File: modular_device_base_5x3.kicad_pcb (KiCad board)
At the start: 2 copper layers, 83.8 x 40.6 mm, 23 parts, among them P1 PWR_JACK_2.5x5.5_SMD_RA, P2 HEADER_01X03_SMD_RA, P3 HEADER_01X03_SMD_RA, P4 HEADER_01X03_SMD_RA, P5 BNC_DOUBLE_RA, P6 HEADER_01X02_SMD_RA, P7 HEADER_01X02_SMD_RA, SW1 KT_SWITCH

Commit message: footprints: -> modular_device_base_5x3:.
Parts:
- MDB1: footprint footprints:MODULAR_DEVICE_BASE_5X3_FEMALE -> modular_device_base_5x3:MODULAR_DEVICE_BASE_5X3_FEMALE
- TEENSY1: footprint footprints:TEENSY_3.2 -> modular_device_base_5x3:TEENSY_3.2
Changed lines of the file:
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@@
     (pad 1 thru_hole circle (at 0 0) (size 3.556 3.556) (drill 3.302) (layers *.Cu *.Mask F.SilkS))
   )
-  (module footprints:MODULAR_DEVICE_BASE_5X3_FEMALE (layer F.Cu)
+  (module modular_device_base_5x3:MODULAR_DEVICE_BASE_5X3_FEMALE (layer F.Cu)
     (at 95.25 99.695)
     (fp_text reference MDB1 (at 0 0) (layer F.SilkS) hide
@@
     (pad "" thru_hole circle (at 22.86 -17.78) (size 3.556 3.556) (drill 3.302) (layers *.Cu *.Mask F.SilkS))
   )
-  (module footprints:TEENSY_3.2 (layer B.Cu)
+  (module modular_device_base_5x3:TEENSY_3.2 (layer B.Cu)
     (at 95.25 99.695 270)
     (fp_text reference TEENSY1 (at 0 -19.05 270) (layer B.SilkS)

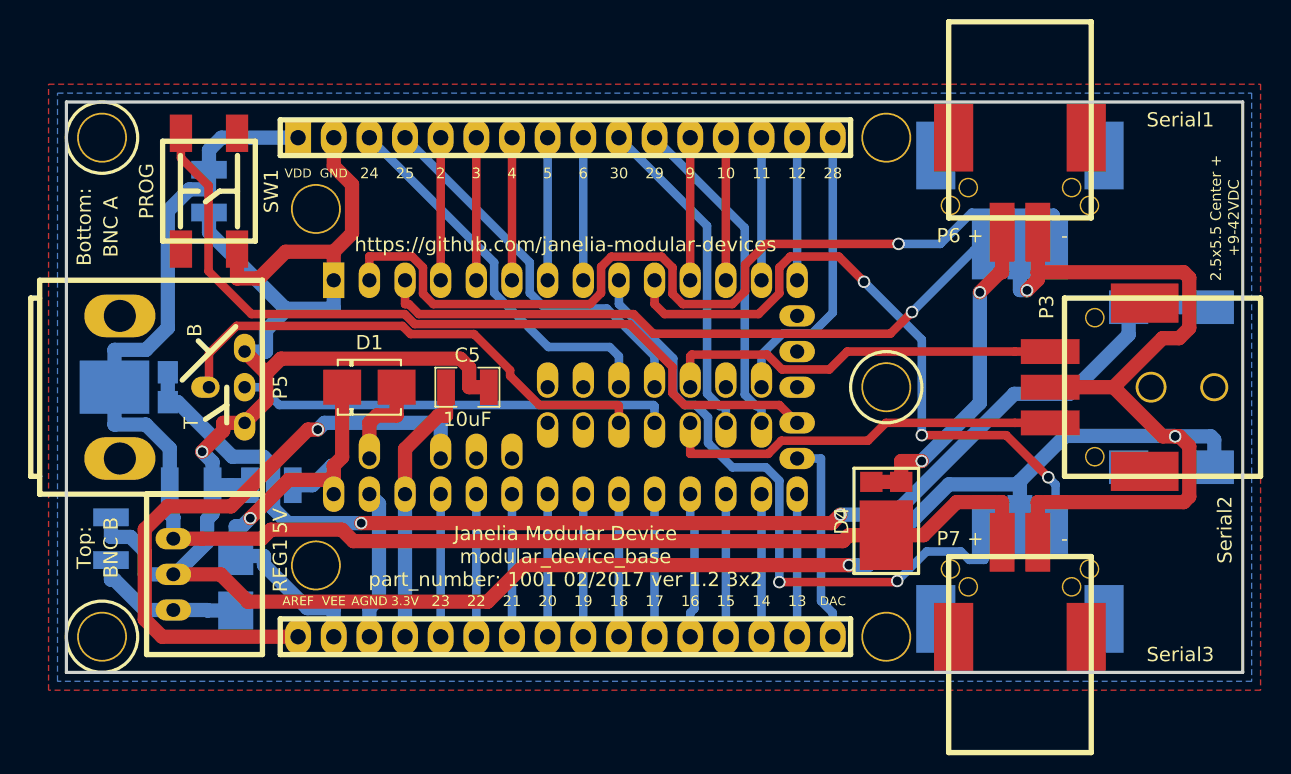
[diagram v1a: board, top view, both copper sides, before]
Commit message: Added TEENSY_3.5 footprint.
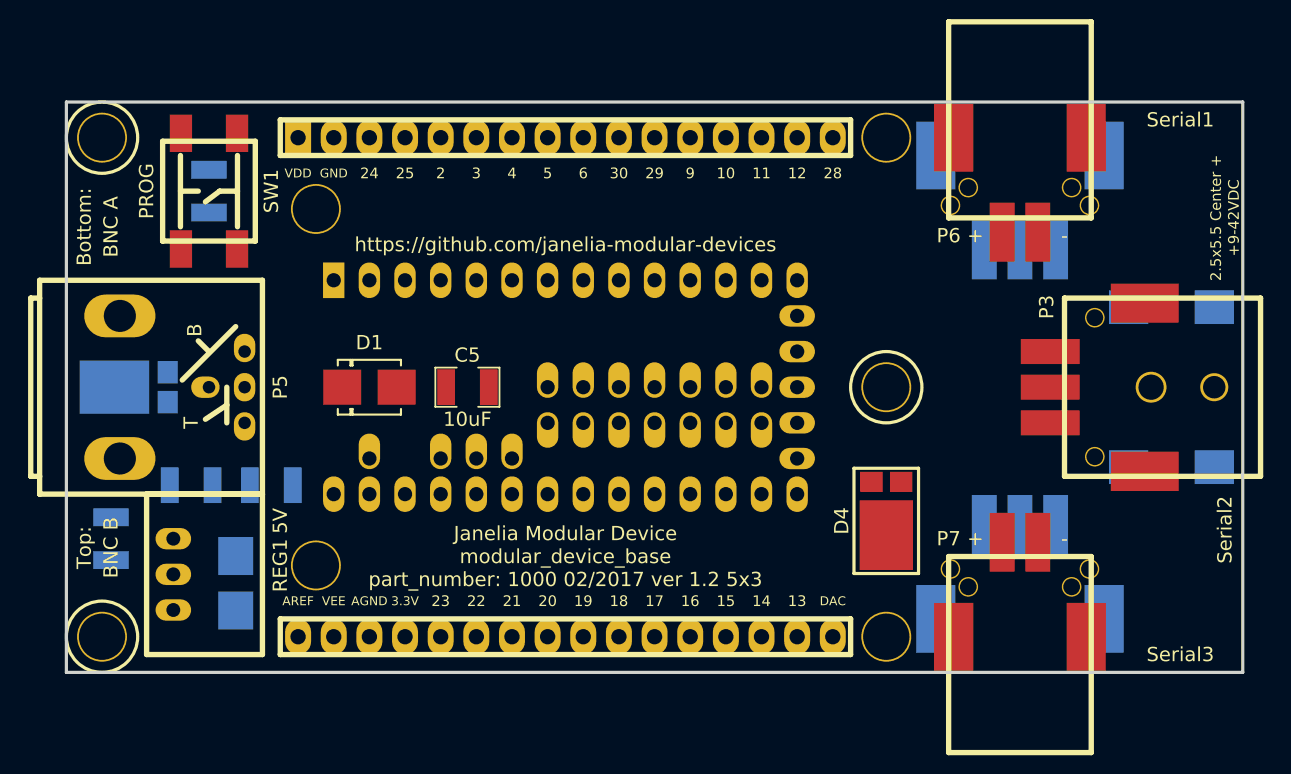
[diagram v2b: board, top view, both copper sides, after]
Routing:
- net GND: track 233.6 -> 0.00 mm, vias 4 -> 0
- net VDD: track 106.1 -> 0.00 mm
- net VAA: track 89.5 -> 0.00 mm, vias 2 -> 0
- net /RX1: track 64.5 -> 0.00 mm, vias 1 -> 0
- net /PROG: track 58.2 -> 0.00 mm
- net /TX3: track 46.9 -> 0.00 mm, vias 3 -> 0
- net /RX3: track 46.4 -> 0.00 mm, vias 2 -> 0
- net /TX1: track 46.3 -> 0.00 mm, vias 1 -> 0
- net /AREF: track 44.6 -> 0.00 mm, vias 1 -> 0
- net /BNC_A: track 36.2 -> 0.00 mm
- net VEE: track 34.8 -> 0.00 mm, vias 1 -> 0
- net /BNC_B: track 31.0 -> 0.00 mm
- net /RX2: track 28.9 -> 0.00 mm
- net /TX2: track 28.8 -> 0.00 mm
- net /D25: track 27.7 -> 0.00 mm
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- removed copper zone on B.Cu, net GND
- removed copper zone on F.Cu, net GND
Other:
- board text added: "Janelia Modular Device modular_device_base part_number: 1000 02/2017 ver 1.2 5x3"
- board text removed: "Janelia Modular Device modular_device_base part_number: 1001 02/2017 ver 1.2 3x2"

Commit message: Progress towards new modifications.
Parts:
- added D5: diode_schottky_45V_10A, modular_device_base_5x3:CFP15, F.Cu at (171.4, 99.7)
- added E1: TEENSY_ETHERNET, footprints:TEENSY_ETHERNET, B.Cu at (153.0, 84.5)
- added MH4: MNT_HOLE, modular_device_base_5x3:MOUNTING_HOLE_4-40, F.Cu at (141.0, 121.9)
- added P10: HEADER_01X02_SMD_RA, modular_device_base_5x3:Header_2_Pin_SMD_RA, F.Cu at (62.2, 83.8)
- added P8: HEADER_01X02_SMD_RA, modular_device_base_5x3:Header_2_Pin_SMD_RA, F.Cu at (191.8, 84.5)
- added P9: HEADER_01X03_SMD_RA, modular_device_base_5x3:Header_3_Pin_SMD_RA, B.Cu at (63.5, 83.8)
- D3: moved to F.Cu
- MDB1: value modular_device_base_5x3_FEMALE -> MODULAR_DEVICE_BASE_5x3_FEMALE; footprint modular_device_base_5x3:MODULAR_DEVICE_BASE_5X3_FEMALE -> footprints:MODULAR_DEVICE_BASE_5X3_FEMALE
- P1: value PWR_JACK_2.5x5.5_SMD_RA -> PWR_JACK_2.5x5.5; footprint modular_device_base_5x3:DCJACK_2PIN_HIGHCURRENT_SMD_RA -> footprints:DCJACK_2PIN_HIGHCURRENT
- P2: value HEADER_01X03_SMD_RA -> BNC_DOUBLE_RA; footprint modular_device_base_5x3:Header_3_Pin_SMD_RA -> modular_device_base_5x3:BNC_DOUBLE; moved to F.Cu
- P3: moved to B.Cu
- P4: value HEADER_01X03_SMD_RA -> HEADER_01X02_SMD_RA; footprint modular_device_base_5x3:Header_3_Pin_SMD_RA -> modular_device_base_5x3:Header_2_Pin_SMD_RA; moved to F.Cu
- P5: value BNC_DOUBLE_RA -> HEADER_01X03_SMD_RA; footprint modular_device_base_5x3:BNC_DOUBLE -> modular_device_base_5x3:Header_3_Pin_SMD_RA; moved to B.Cu
- P7: value HEADER_01X02_SMD_RA -> HEADER_01X03_SMD_RA; footprint modular_device_base_5x3:Header_2_Pin_SMD_RA -> modular_device_base_5x3:Header_3_Pin_SMD_RA; moved to B.Cu
- TEENSY1: value TEENSY_3_2 -> TEENSY_3.5; footprint modular_device_base_5x3:TEENSY_3.2 -> footprints:TEENSY_3.5
- moved P5 119.2 mm to (179.1, 128.9), turned to 0 degrees
- moved D3 112.4 mm to (176.5, 99.7), turned to 0 degrees
- moved P7 71.0 mm to (190.5, 84.5), turned to 90 degrees
- moved P6 70.5 mm to (179.1, 130.2), turned to 180 degrees
- moved P4 69.2 mm to (178.4, 69.2)
- moved P2 66.2 mm to (63.5, 99.7), turned to 90 degrees
- moved P1 55.9 mm to (194.3, 99.7), turned to 90 degrees
- moved P3 51.1 mm to (178.4, 70.5), turned to 180 degrees
- moved D4 49.2 mm to (166.4, 99.7)
- moved MH3 31.9 mm to (141.0, 77.5)
- moved C3 13.3 mm to (69.8, 72.4)
- moved SW1 13.3 mm to (69.8, 72.4)
- moved MH2 12.7 mm to (62.2, 130.2)
- moved MH1 12.7 mm to (62.2, 69.2)
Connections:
- P2 pad 1: /RX1 -> /BNC_A
- P2 pad 3: /TX1 -> /BNC_B
- P3 pad 1: /RX2 -> /RX1
- P3 pad 3: /TX2 -> /TX1
- P4 pad 1: /RX3 -> VCC
- P5 pad 1: /BNC_A -> /RX3
- P5 pad 3: /BNC_B -> /TX3
- P6 pad 1: VCC -> GND
- P6 pad 2: GND -> VDD
- P7 pad 1: GND -> /RX2
- P7 pad 2: VDD -> GND
- TEENSY1 pad 10: /D10 -> /TX2
- TEENSY1 pad 24: /D24 -> /E_CLK
- TEENSY1 pad 25: /D25 -> /E_RXER
- TEENSY1 pad 26: /RX2 -> /E_RXDV
- TEENSY1 pad 27: (no net) -> /E_TXEN
- TEENSY1 pad 28: /D28 -> /E_TXD0
- TEENSY1 pad 3: /D3 -> /E_RXD1
- TEENSY1 pad 31: /TX2 -> /RX4
- TEENSY1 pad 32: /BNC_B -> /TX4
- TEENSY1 pad 33: /BNC_A -> /D33
- TEENSY1 pad 4: /D4 -> /E_RXD0
- TEENSY1 pad 9: /D9 -> /RX2
- TEENSY1 pad A10: (no net) -> /A10
- TEENSY1 pad A11: (no net) -> /A11
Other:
- board size 83.8 x 40.6 mm -> 134.6 x 66 mm

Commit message: Finished design ver 1.0.
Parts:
- moved MH3 51.5 mm to (191.8, 69.2)
- moved MH4 51.5 mm to (191.8, 130.2)
- moved D4 10.4 mm to (174.6, 93.3), turned to 270 degrees
- moved D3 6.63 mm to (174.6, 106.0), turned to 270 degrees
- moved E1 6.35 mm to (159.4, 84.5)
- moved D5 3.18 mm to (174.6, 99.7), turned to 270 degrees
- moved P7 0.64 mm to (190.5, 83.8)
- moved P8 0.64 mm to (191.8, 83.8)
- moved P5 0.63 mm to (178.4, 128.9)
- moved P6 0.63 mm to (178.4, 130.2)
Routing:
- net GND: track 0.00 -> 337.7 mm, vias 0 -> 4
- net VDD: track 0.00 -> 206.6 mm, vias 0 -> 2
- net /RX1: track 0.00 -> 110.5 mm, vias 0 -> 1
- net /TX2: track 0.00 -> 106.8 mm, vias 0 -> 1
- net /TX1: track 0.00 -> 103.2 mm, vias 0 -> 1
- net /TX3: track 0.00 -> 95.7 mm, vias 0 -> 1
- net /RX3: track 0.00 -> 93.5 mm, vias 0 -> 1
- net /RX4: track 0.00 -> 91.0 mm, vias 0 -> 2
- net /PROG: track 0.00 -> 86.7 mm
- net /E_RXD1: track 0.00 -> 84.9 mm
- net /RX2: track 0.00 -> 83.0 mm, vias 0 -> 1
- net /TX4: track 0.00 -> 82.7 mm, vias 0 -> 2
- net /E_RXD0: track 0.00 -> 81.3 mm
- net /E_RXDV: track 0.00 -> 61.1 mm
- net /E_RXER: track 0.00 -> 60.4 mm
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- added copper zone on B.Cu, net GND
- added copper zone on F.Cu, net VDD
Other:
- net class Power: trace_width 1.016 -> 1.2192
- board text added: "2.5x5.5 Center + +9-42VDC"
- board text added: "BNC A"
- board text added: "BNC B"
- board text added: "Janelia Modular Device modular_device_base part_number: 1000 02/2017 ver 1.0 5x3"
- board text added: "Serial4"
- board text removed: "+9-42VDC"
- board text removed: "2.5x5.5 Center +"
- board text removed: "Janelia Modular Device modular_device_base part_number: 1000 02/2017 ver 1.2 5x3"

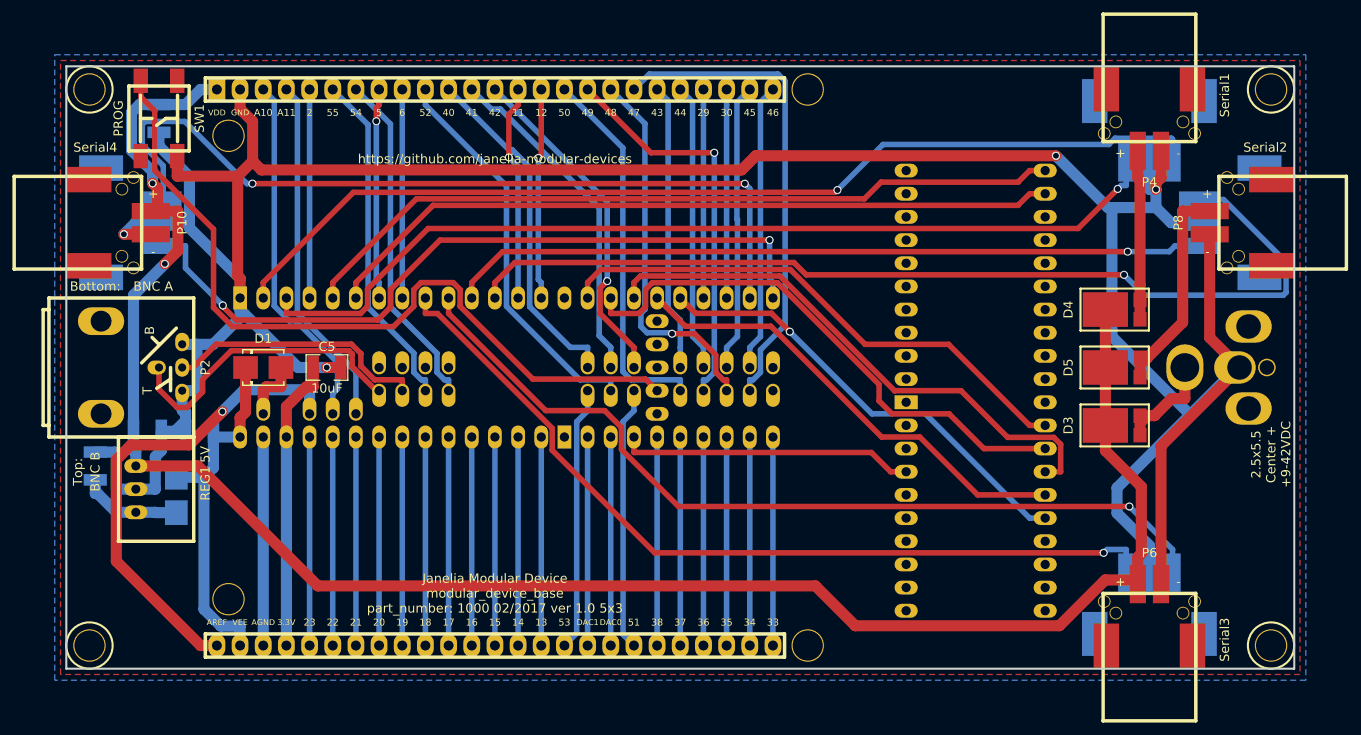
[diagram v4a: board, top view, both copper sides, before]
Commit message: Added components and footprints.
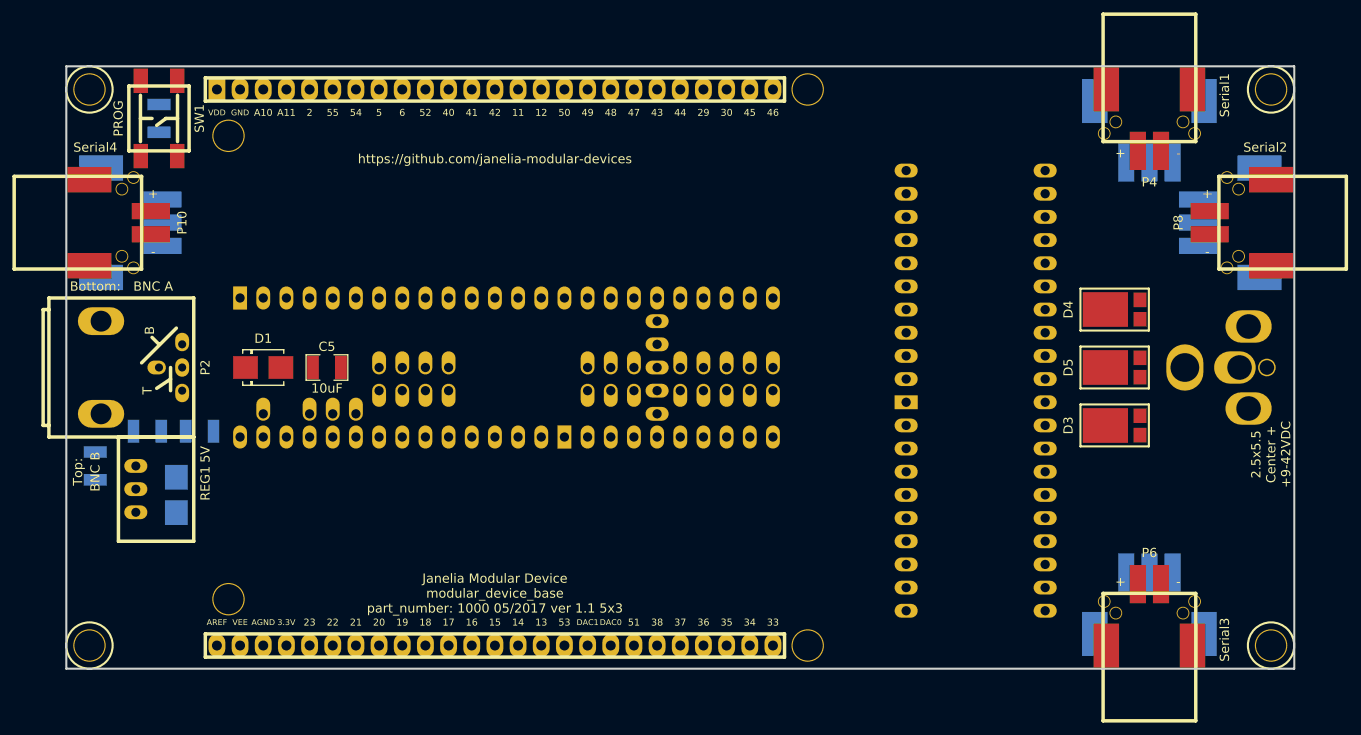
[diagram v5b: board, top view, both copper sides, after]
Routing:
- net GND: track 337.7 -> 0.00 mm, vias 4 -> 0
- net VDD: track 206.6 -> 0.00 mm, vias 2 -> 0
- net /RX1: track 110.5 -> 0.00 mm, vias 1 -> 0
- net /TX2: track 106.8 -> 0.00 mm, vias 1 -> 0
- net /TX1: track 103.2 -> 0.00 mm, vias 1 -> 0
- net /TX3: track 95.7 -> 0.00 mm, vias 1 -> 0
- net /RX3: track 93.5 -> 0.00 mm, vias 1 -> 0
- net /RX4: track 91.0 -> 0.00 mm, vias 2 -> 0
- net /PROG: track 86.7 -> 0.00 mm
- net /E_RXD1: track 84.9 -> 0.00 mm
- net /RX2: track 83.0 -> 0.00 mm, vias 1 -> 0
- net /TX4: track 82.7 -> 0.00 mm, vias 2 -> 0
- net /E_RXD0: track 81.3 -> 0.00 mm
- net /E_RXDV: track 61.1 -> 0.00 mm
- net /E_RXER: track 60.4 -> 0.00 mm
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- removed copper zone on B.Cu, net GND
- removed copper zone on F.Cu, net VDD
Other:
- board text added: "Janelia Modular Device modular_device_base part_number: 1000 05/2017 ver 1.1 5x3"
- board text removed: "Janelia Modular Device modular_device_base part_number: 1000 02/2017 ver 1.0 5x3"

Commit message: Progress towards v1.1.
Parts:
- removed E1: TEENSY_ETHERNET, footprints:TEENSY_ETHERNET
- added C6: 0.1uF, footprints:SM1210, F.Cu at (282.9, 63.9)
- added D10: diode_schottky_45V_10A, modular_device_base_5x3:CFP15, F.Cu at (239.1, 77.4)
- added D11: diode_schottky_45V_10A, modular_device_base_5x3:CFP15, F.Cu at (239.1, 88.8)
- added D12: diode_schottky_45V_10A, modular_device_base_5x3:CFP15, F.Cu at (258.2, 77.4)
- added D13: diode_schottky_45V_10A, modular_device_base_5x3:CFP15, F.Cu at (258.2, 66.1)
- added D6: diode_schottky_45V_10A, modular_device_base_5x3:CFP15, F.Cu at (220.0, 66.1)
- added D7: diode_schottky_45V_10A, modular_device_base_5x3:CFP15, F.Cu at (220.0, 77.4)
- added D8: diode_schottky_45V_10A, modular_device_base_5x3:CFP15, F.Cu at (239.1, 66.1)
- added D9: diode_schottky_45V_10A, modular_device_base_5x3:CFP15, F.Cu at (220.0, 88.8)
- added L1: LED_5V_RED_RA, footprints:LED_555-2XXX, F.Cu at (274.0, 64.4)
- added L2: LED_5V_GRN_RA, footprints:LED_555-2XXX, F.Cu at (230.3, 98.6)
- added L3: LED_5V_YEL_RA, footprints:LED_555-2XXX, F.Cu at (273.8, 73.0)
- added MH5: MNT_HOLE, modular_device_base_5x3:MOUNTING_HOLE_4-40, F.Cu at (254.8, 87.9)
- added MH6: MNT_HOLE, modular_device_base_5x3:MOUNTING_HOLE_4-40, F.Cu at (242.7, 99.3)
- added R1: 6.19k, footprints:SM1210, F.Cu at (263.5, 86.6)
- added SW2: KT_SWITCH, modular_device_base_5x3:KT_SWITCH, F.Cu at (216.2, 99.1)
- added U1: MAX6817, footprints:MAX6817, F.Cu at (251.0, 95.8)
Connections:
- C1 pad 1: VDD -> VPP
- C3 pad 1: VDD -> VPP
- D3 pad 1: VDD -> VPP
- D4 pad 1: VDD -> VPP
- D4 pad 2: VCC -> VDD
- D5 pad 2: VDDA -> VPP
- P10 pad 2: VDD -> VSSA
- P6 pad 2: VDD -> VSS
- REG1 pad 1: VDD -> VPP
- SW1 pad 2: /PROG -> /BTN_A
- TEENSY1 pad 24: /E_CLK -> /BTN_A_D
- TEENSY1 pad 25: /E_RXER -> /BTN_B_D
- TEENSY1 pad 26: /E_RXDV -> /LED_GRN
- TEENSY1 pad 27: /E_TXEN -> /LED_YEL
- TEENSY1 pad 28: /E_TXD0 -> (no net)
- TEENSY1 pad 3: /E_RXD1 -> (no net)
- TEENSY1 pad 39: /E_TXD1 -> (no net)
- TEENSY1 pad 4: /E_RXD0 -> (no net)
- TEENSY1 pad PROG: /PROG -> (no net)

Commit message: More progress towards v1.1.
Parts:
- added P11: HEADER_01X03_RA, footprints:Header_3_Pin_RA, B.Cu at (187.3, 110.5)
- D11, D13, D5, D7, D9, L1: moved to B.Cu
- moved L3 211.2 mm to (70.5, 130.2), turned to 180 degrees
- moved L2 165.4 mm to (67.9, 130.2), turned to 180 degrees
- moved SW2 149.4 mm to (69.2, 72.4), turned to 270 degrees
- moved MH5 147.1 mm to (108.0, 79.4)
- moved MH6 101.5 mm to (146.1, 130.2)
- moved L1 101.1 mm to (191.8, 123.2), turned to 90 degrees
- moved D13 98.9 mm to (169.5, 109.9), turned to 270 degrees
- moved D12 95.3 mm to (169.5, 112.4), turned to 270 degrees
- moved D8 80.9 mm to (169.5, 107.3), turned to 270 degrees
- moved D10 72.3 mm to (169.5, 97.2), turned to 270 degrees
- moved D11 70.4 mm to (169.5, 99.7), turned to 270 degrees
- moved D6 56.8 mm to (169.5, 92.1), turned to 270 degrees
- moved D7 53.3 mm to (169.5, 94.6), turned to 270 degrees
- moved D9 52.9 mm to (169.5, 104.8), turned to 270 degrees
- moved SW1 51.4 mm to (69.2, 123.8), turned to 180 degrees
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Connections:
- R1 pad 2: Net-(L1-Pad1) -> Net-(P11-Pad2)
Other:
- board size 134.6 x 66 mm -> 135.9 x 67.3 mm
- board text added: "+9-42VDC"
- board text added: "1"
- board text added: "2"
- board text added: "3"
- board text added: "4"
- board text added: "G"
- board text added: "RX4"
- board text added: "TX4"
- board text added: "Top: BNC B Bot: BNC A"
- board text removed: "BNC A"
- board text removed: "BNC B"
- board text removed: "Bottom:"
- board text removed: "Serial1"
- board text removed: "Serial2"
- board text removed: "Serial3"
- board text removed: "Serial4"
- board text removed: "Top:"

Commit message: Completed v1.1.
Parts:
- added MH7: MNT_HOLE, modular_device_base_5x3:MOUNTING_HOLE_4-40, F.Cu at (146.1, 69.2)
- added MH8: MNT_HOLE, modular_device_base_5x3:MOUNTING_HOLE_4-40, F.Cu at (146.1, 130.2)
- C6, R1, U1: moved to B.Cu
- moved C6 219.1 mm to (66.7, 99.7), turned to 90 degrees
- moved U1 189.4 mm to (61.6, 99.7)
- moved C3 120.8 mm to (168.3, 83.2), turned to 0 degrees
- moved R1 99.7 mm to (168.3, 116.2)
- moved MH6 41.0 mm to (108.0, 114.9)
- moved C2 21.5 mm to (65.4, 110.5), turned to 270 degrees
- moved C1 9.44 mm to (65.4, 115.6), turned to 90 degrees
- moved D2 7.01 mm to (71.1, 106.7), turned to 180 degrees
- moved C4 6.84 mm to (76.8, 113.0)
- moved MH5 5.08 mm to (108.0, 84.5)
- moved REG1 4.44 mm to (71.8, 113.0), turned to 90 degrees
- turned SW2 to 90 degrees
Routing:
- net GND: track 0.00 -> 407.0 mm, vias 0 -> 2
- net VPP: track 0.00 -> 168.6 mm, vias 0 -> 2
- net VSSA: track 0.00 -> 129.9 mm, vias 0 -> 1
- net /LED_YEL: track 0.00 -> 129.0 mm, vias 0 -> 1
- net /RX1: track 0.00 -> 116.6 mm, vias 0 -> 2
- net /RX2: track 0.00 -> 115.5 mm, vias 0 -> 1
- net VDD: track 0.00 -> 115.1 mm, vias 0 -> 1
- net /TX1: track 0.00 -> 105.7 mm, vias 0 -> 2
- net /TX3: track 0.00 -> 95.4 mm, vias 0 -> 2
- net /LED_GRN: track 0.00 -> 95.0 mm
- net /RX3: track 0.00 -> 93.1 mm, vias 0 -> 1
- net /TX2: track 0.00 -> 90.8 mm, vias 0 -> 1
- net /RX4: track 0.00 -> 76.0 mm, vias 0 -> 2
- net /TX4: track 0.00 -> 71.9 mm, vias 0 -> 2
- net /D48: track 0.00 -> 65.4 mm
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- added copper zone on B.Cu, net GND
- added copper zone on F.Cu, net GND
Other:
- board text added: "LED"
- board text added: "OFF"
- board text added: "ON"
- board text added: "R"
- board text added: "RX2"
- board text added: "RX3"
- board text added: "TX1"
- board text added: "TX3"
- board text added: "Y"
